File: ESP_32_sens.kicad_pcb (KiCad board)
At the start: 4 copper layers, 105 x 50 mm, 79 parts, among them J201 Conn_01x04_Pin, J301 USB_C_Receptacle_USB2.0_16P, SW201 SW_Push, U201 BMI323, U202 ESP32-S3, U203 MX25L6433FM2I-08G, U204 ESP-PSRAM32, U301 USBLC6-2SC6, U302 HT7533-1, U303 TLV62569DBV, U401 TESEO-LIV3R, U402 BGA725L6E6327FTSA1, Y201 Crystal_GND24

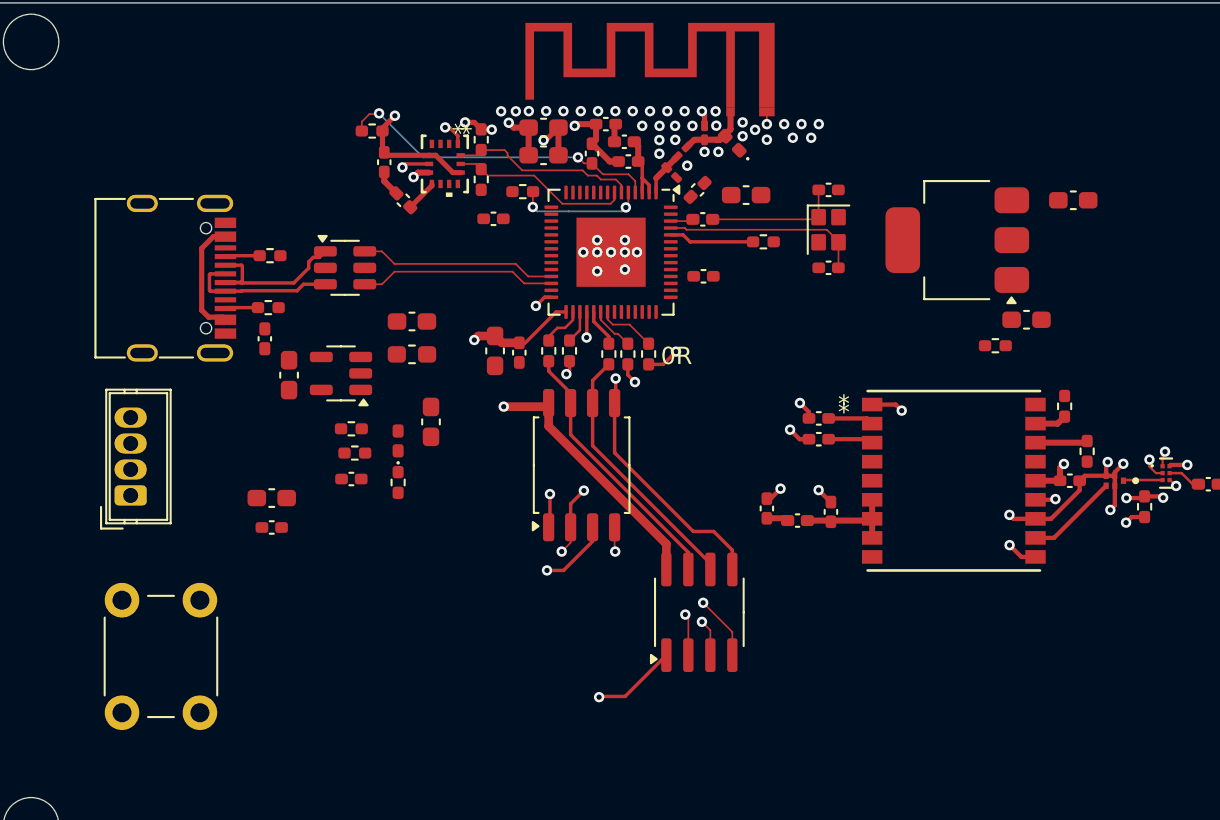
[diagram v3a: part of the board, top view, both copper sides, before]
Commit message: finished power routing
finished power routing, gps antenna left
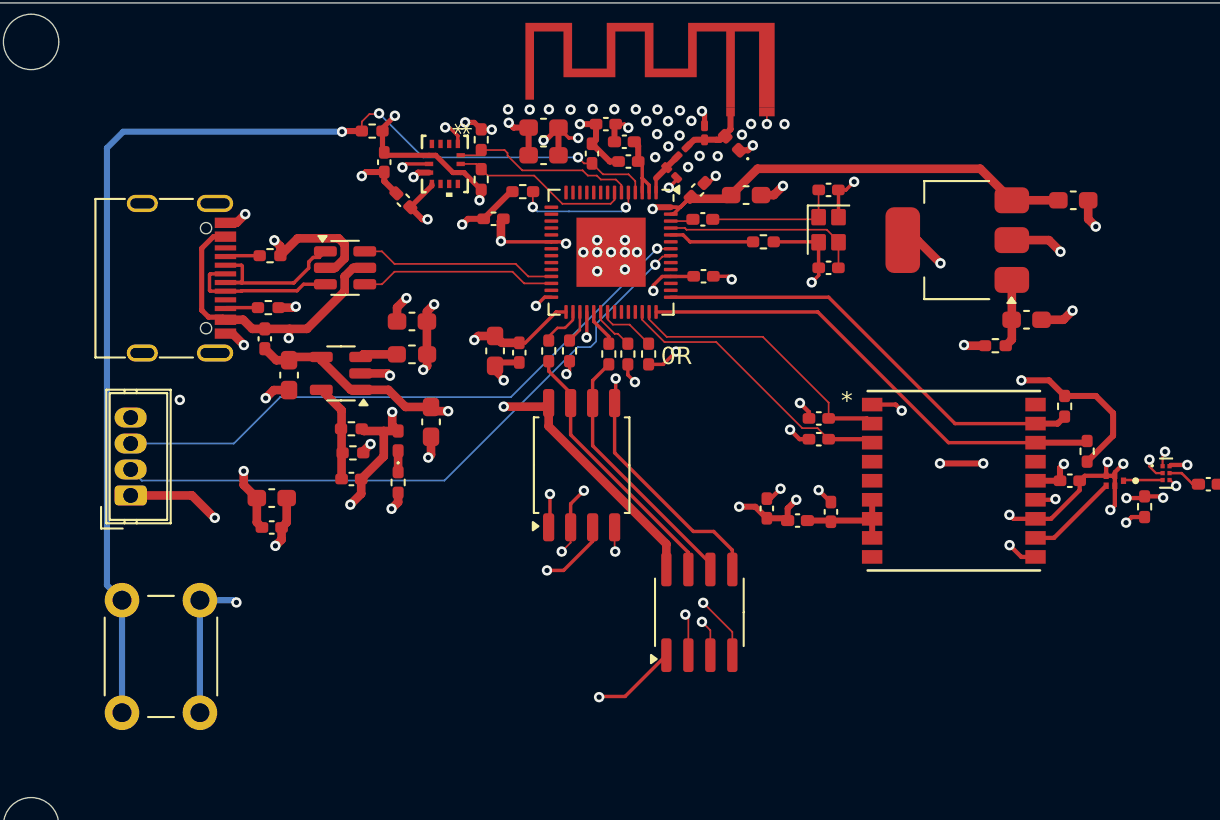
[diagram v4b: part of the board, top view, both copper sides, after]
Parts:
- moved R305 0.11 mm to (133.6, 101.0)
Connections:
- U202 pad 40: UART2_TX -> UART2_RX
- U202 pad 41: UART2_RX -> UART2_TX
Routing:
- net +3.3V: track 21.6 -> 129.0 mm, vias 4 -> 20
- net +5V: track 0.00 -> 77.6 mm, vias 0 -> 2
- net GND: track 49.4 -> 115.3 mm, vias 64 -> 80
- net /MCU [2]/Chip_pu: track 18.8 -> 66.9 mm, vias 2 -> 3
- net +3.3VA: track 1.86 -> 44.2 mm, vias 0 -> 2
- net UART_TX: track 0.00 -> 37.5 mm, vias 0 -> 1
- net UART_RX: track 0.00 -> 35.9 mm, vias 0 -> 1
- net I2C_SDA_2: track 3.02 -> 28.1 mm
- net I2C_SCL_2: track 1.85 -> 25.9 mm
- net VBUS: track 6.83 -> 30.1 mm, vias 0 -> 2
- net UART2_RX: track 2.60 -> 16.7 mm
- net UART2_TX: track 2.64 -> 16.3 mm
- net /PSU [3]/BUCK_FB: track 0.00 -> 5.63 mm
- net /PSU [3]/+5V_FILT: track 0.00 -> 3.95 mm
- net /PSU [3]/BUCK_SW: track 0.00 -> 2.15 mm
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
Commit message: minor changes
minor changes
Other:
- board text added: "Flatrim Dreshaj Motion Tracker V1 AMNTL-CNDE"
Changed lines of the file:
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@@
 		)
 	)
+	(gr_text "Flatrim Dreshaj \nMotion Tracker V1\nAMNTL-CNDE"
+		(at 210.1 83.2 0)
+		(layer "B.SilkS")
+		(effects
+			(font
+				(size 1.5 1.5)
+				(thickness 0.3)
+				(bold yes)
+			)
+			(justify left bottom mirror)
+		)
+	)
 	(segment
 		(start 138.1 100.0625)
@@
 		(min_thickness 0.25)
 		(filled_areas_thickness no)
-		(fill yes
+		(fill
 			(thermal_gap 0.5)
 			(thermal_bridge_width 0.5)
@@
 		(polygon
 			(pts
-				(xy 154.99 81.6) (xy 156.7 81.6) (xy 156.7 81.1) (xy 158.2 81.1) (xy 216 81.3) (xy 215.2 120.2)
+				(xy 154.99 81.6) (xy 156.7 81.6) (xy 156.7 81.1) (xy 182.1 81.1) (xy 215.2 81.196667) (xy 215.2 120.2)
 				(xy 116.7 120) (xy 116.9 80) (xy 139.9 79.9) (xy 139.9 80.8) (xy 154.99 80.8)
 			)

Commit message: minor changes
minor changes
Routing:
- net Net-(AE402-A): track 27.2 -> 0.00 mm
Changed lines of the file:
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@@
-	)
-	(segment
-		(start 205.766301 97.4837)
-		(end 191.4838 97.4837)
-		(width 0.355)
-		(layer "F.Cu")
-		(net 26)
-	)
-	(segment
-		(start 209.650001 93.6)
-		(end 205.766301 97.4837)
-		(width 0.355)
-		(layer "F.Cu")
-		(net 26)
-	)
-	(segment
-		(start 191.4838 97.4837)
-		(end 186.2675 102.7)
-		(width 0.355)
-		(layer "F.Cu")
-		(net 26)
 	)
 	(segment
@@
 		(min_thickness 0.25)
 		(filled_areas_thickness no)
-		(fill
+		(fill yes
 			(thermal_gap 0.5)
 			(thermal_bridge_width 0.5)

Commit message: changes
changes made
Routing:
- net Net-(AE402-A): track 0.00 -> 2.47 mm
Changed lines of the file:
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@@
 		)
 		(fp_text user "*"
-			(at -11.539999 -9.0016 270)
-			(unlocked yes)
+			(at -11.539999 -9.0016 90)
 			(layer "F.SilkS")
 			(effects
@@
 		)
 		(fp_text user "*"
-			(at -11.539999 -9.0016 90)
+			(at -11.539999 -9.0016 270)
+			(unlocked yes)
 			(layer "F.SilkS")
 			(effects
@@
 		)
 		(pad "1" smd rect
-			(at -9 -9.0016 270)
-			(size 7.0104 7.0104)
+			(at 0 11.948401 270)
+			(size 1.397 1.397)
 			(layers "F.Cu" "F.Mask" "F.Paste")
 			(net 26 "Net-(AE402-A)")
@@
 		)
 		(pad "8" smd rect
-			(at 0 11.948401 270)
-			(size 1.397 1.397)
+			(at -9 -9.0016 270)
+			(size 7.0104 7.0104)
 			(layers "F.Cu" "F.Mask" "F.Paste")
 		)
@@
 	)
 	(segment
+		(start 186.2675 102.7)
+		(end 188.6 102.7)
+		(width 0.355)
+		(layer "F.Cu")
+		(net 26)
+	)
+	(segment
+		(start 188.6 102.7)
+		(end 188.7 102.6)
+		(width 0.355)
+		(layer "F.Cu")
+		(net 26)
+	)
+	(segment
